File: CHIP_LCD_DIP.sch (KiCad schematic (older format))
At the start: 22 parts, among them CON1 C.H.I.P., CON2 Power, IC1 74LVC138, IC2 DS2431, IC3 AP3032, IC4 74AHC1G08, P1 GPIO, P2 UART, P3 Pwr SW, P5 LCD

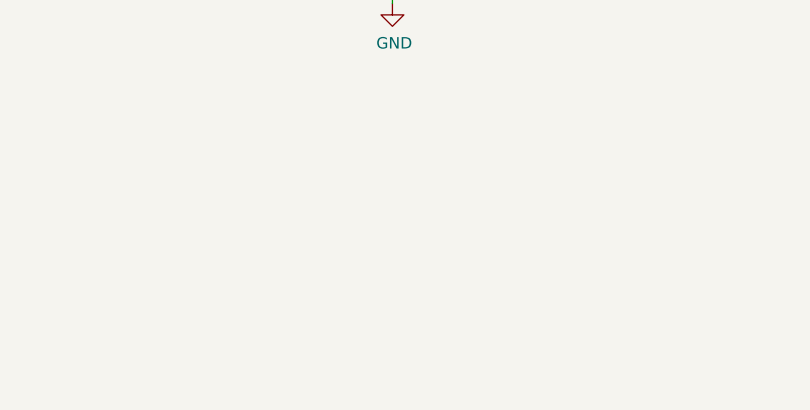
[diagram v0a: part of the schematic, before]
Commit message: Added connector to go to optional capacitive touch board.
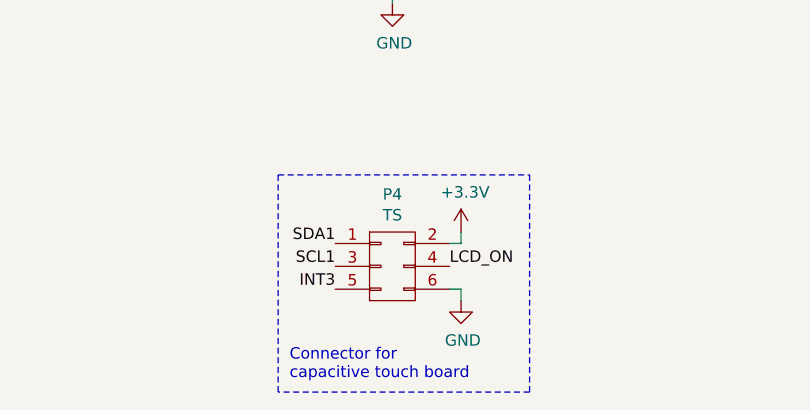
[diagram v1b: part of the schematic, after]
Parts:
- added P4: TS, connectors:02x03_Header_0.05, symbol CONN_02X03
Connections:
- net +3V3: now also P4.2 (P2)
- net GND: now also P4.6 (P6)
- net INT3: now also P4.5 (P5)
- net LCD_ON: now also P4.4 (P4)
- net SCL1: now also P4.3 (P3)
- net SDA1: now also P4.1 (P1)
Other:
- note added: "Connector for\ncapacitive touch board"
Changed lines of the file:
@@
 Sheet 1 1
 Title "C.H.I.P. LCD Adapter & SPI Expander"
-Date "2016-09-01"
-Rev "2"
+Date "2016-09-02"
+Rev "3"
 Comp "Cody Nybo"
 Comment1 ""
@@
 Y2
 $Comp
-L +3.3V #PWR11
+L +3.3V #PWR01
 U 1 1 570D8EAB
 P 3500 5000
-F 0 "#PWR11" H 3500 4850 50  0001 C CNN
+F 0 "#PWR01" H 3500 4850 50  0001 C CNN
 F 1 "+3.3V" H 3518 5174 50  0000 C CNN
 F 2 "" H 3500 5000 60  0000 C CNN
@@
 $EndComp
 $Comp
-L +5V #PWR10
+L +5V #PWR02
 U 1 1 570D8ED5
 P 3250 5000
-F 0 "#PWR10" H 3250 4850 50  0001 C CNN
+F 0 "#PWR02" H 3250 4850 50  0001 C CNN
 F 1 "+5V" H 3268 5174 50  0000 C CNN
 F 2 "" H 3250 5000 60  0000 C CNN
@@
 $EndComp
 $Comp
-L +3.3V #PWR1
+L +3.3V #PWR03
 U 1 1 570D8F46
 P 5200 950
-F 0 "#PWR1" H 5200 800 50  0001 C CNN
+F 0 "#PWR03" H 5200 800 50  0001 C CNN
 F 1 "+3.3V" H 5218 1124 50  0000 C CNN
 F 2 "" H 5200 950 60  0000 C CNN
@@
 $EndComp
 $Comp
-L GND #PWR15
+L GND #PWR04
 U 1 1 570D9535
 P 2250 6000
-F 0 "#PWR15" H 2250 5750 50  0001 C CNN
+F 0 "#PWR04" H 2250 5750 50  0001 C CNN
 F 1 "GND" H 2258 5826 50  0000 C CNN
 F 2 "" H 2250 6000 60  0000 C CNN
@@
 $EndComp
 $Comp
-L GND #PWR6
+L GND #PWR05
 U 1 1 570D971F
 P 5200 2450
-F 0 "#PWR6" H 5200 2200 50  0001 C CNN
+F 0 "#PWR05" H 5200 2200 50  0001 C CNN
 F 1 "GND" H 5208 2276 50  0000 C CNN
 F 2 "" H 5200 2450 60  0000 C CNN
@@
 $EndComp
 $Comp
-L GND #PWR13
+L GND #PWR06
 U 1 1 570E7088
 P 5000 5400
-F 0 "#PWR13" H 5000 5150 50  0001 C CNN
+F 0 "#PWR06" H 5000 5150 50  0001 C CNN
 F 1 "GND" H 5008 5226 50  0000 C CNN
 F 2 "" H 5000 5400 60  0000 C CNN
@@
 $EndComp
 $Comp
-L GND #PWR14
+L GND #PWR07
 U 1 1 570EB8AA
 P 4000 5500
-F 0 "#PWR14" H 4000 5250 50  0001 C CNN
+F 0 "#PWR07" H 4000 5250 50  0001 C CNN
 F 1 "GND" H 4008 5326 50  0000 C CNN
 F 2 "" H 4000 5500 60  0000 C CNN
@@
 Mute
 $Comp
-L +1V8 #PWR12
+L +1V8 #PWR08
 U 1 1 570F8C40
 P 3750 5000
-F 0 "#PWR12" H 3750 4850 50  0001 C CNN
+F 0 "#PWR08" H 3750 4850 50  0001 C CNN
 F 1 "+1V8" H 3768 5174 50  0000 C CNN
 F 2 "" H 3750 5000 60  0000 C CNN
@@
 $EndComp
 $Comp
-L +3.3V #PWR2
+L +3.3V #PWR09
 U 1 1 570F99ED
 P 9050 1500
-F 0 "#PWR2" H 9050 1350 50  0001 C CNN
+F 0 "#PWR09" H 9050 1350 50  0001 C CNN
 F 1 "+3.3V" H 9068 1674 50  0000 C CNN
 F 2 "" H 9050 1500 60  0000 C CNN
@@
 $EndComp
 $Comp
-L GND #PWR9
+L GND #PWR010
 U 1 1 570FA672
 P 8450 4800
-F 0 "#PWR9" H 8450 4550 50  0001 C CNN
+F 0 "#PWR010" H 8450 4550 50  0001 C CNN
 F 1 "GND" H 8458 4626 50  0000 C CNN
 F 2 "" H 8450 4800 60  0000 C CNN
@@
 NoConn ~ 9800 4650
 $Comp
-L GND #PWR4
+L GND #PWR011
 U 1 1 5711414E
 P 9050 1950
-F 0 "#PWR4" H 9050 1700 50  0001 C CNN
+F 0 "#PWR011" H 9050 1700 50  0001 C CNN
 F 1 "GND" H 9058 1776 50  0000 C CNN
 F 2 "" H 9050 1950 60  0000 C CNN
@@
 	1150 1850 1600 1850
 $Comp
-L GND #PWR5
+L GND #PWR012
 U 1 1 5770C9CC
 P 1200 2000
-F 0 "#PWR5" H 1200 1750 50  0001 C CNN
+F 0 "#PWR012" H 1200 1750 50  0001 C CNN
 F 1 "GND" H 1208 1826 50  0000 C CNN
 F 2 "" H 1200 2000 60  0000 C CNN
@@
 Connection ~ 1200 1850
 $Comp
-L +3.3V #PWR3
+L +3.3V #PWR013
 U 1 1 5770D995
 P 1200 1550
-F 0 "#PWR3" H 1200 1400 50  0001 C CNN
+F 0 "#PWR013" H 1200 1400 50  0001 C CNN
 F 1 "+3.3V" H 1218 1724 50  0000 C CNN
 F 2 "" H 1200 1550 60  0000 C CNN
@@
 Connection ~ 8100 4750
 $Comp
-L +3.3V #PWR8
+L +3.3V #PWR014
 U 1 1 57721227
 P 7300 4200
-F 0 "#PWR8" H 7300 4050 50  0001 C CNN
+F 0 "#PWR014" H 7300 4050 50  0001 C CNN
 F 1 "+3.3V" H 7318 4374 50  0000 C CNN
 F 2 "" H 7300 4200 60  0000 C CNN
@@
 XIO3
 $Comp
-L +5V #PWR7
+L +5V #PWR015
 U 1 1 57C03EA0
 P 8100 3600
-F 0 "#PWR7" H 8100 3450 50  0001 C CNN
+F 0 "#PWR015" H 8100 3450 50  0001 C CNN
 F 1 "+5V" H 8118 3774 50  0000 C CNN
 F 2 "" H 8100 3600 60  0000 C CNN
@@
 	1    0    0    -1
 $EndComp
+$Comp
+L CONN_02X03 P4
+U 1 1 57CA09BF
+P 2250 7150
+F 0 "P4" H 2250 7465 50  0000 C CNN
+F 1 "TS" H 2250 7374 50  0000 C CNN
+F 2 "connectors:02x03_Header_0.05" H 2250 7381 60  0001 C CNN
+F 3 "" H 2250 5950 60  0000 C CNN
+	1    2250 7150
+	1    0    0    -1
+$EndComp
+$Comp
+L +3.3V #PWR016
+U 1 1 57CA1873
+P 2550 7000
+F 0 "#PWR016" H 2550 6850 50  0001 C CNN
+F 1 "+3.3V" H 2568 7174 50  0000 C CNN
+F 2 "" H 2550 7000 60  0000 C CNN
+F 3 "" H 2550 7000 60  0000 C CNN
+	1    2550 7000
+	1    0    0    -1
+$EndComp
+$Comp
+L GND #PWR017
+U 1 1 57CA18C0
+P 2550 7300
+F 0 "#PWR017" H 2550 7050 50  0001 C CNN
+F 1 "GND" H 2558 7126 50  0000 C CNN
+F 2 "" H 2550 7300 60  0000 C CNN
+F 3 "" H 2550 7300 60  0000 C CNN
+	1    2550 7300
+	1    0    0    -1
+$EndComp
+Wire Wire Line
+	2500 7250 2550 7250
+Wire Wire Line
+	2550 7250 2550 7300
+Wire Wire Line
+	2500 7050 2550 7050
+Wire Wire Line
+	2550 7050 2550 7000
+Text Label 2000 7050 2    50   ~ 0
+SDA1
+Text Label 2000 7150 2    50   ~ 0
+SCL1
+Text Label 2000 7250 2    50   ~ 0
+INT3
+Text Label 2500 7150 0    50   ~ 0
+LCD_ON
+Wire Notes Line
+	1750 6750 2850 6750
+Wire Notes Line
+	2850 6750 2850 7700
+Wire Notes Line
+	2850 7700 1750 7700
+Wire Notes Line
+	1750 7700 1750 6750
+Text Notes 1800 7650 0    50   ~ 0
+Connector for\ncapacitive touch board
 $EndSCHEMATC

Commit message: Updated files. Added source code. Added pdf copies of design files.
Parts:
- C4: footprint capacitor_smd:C_0805 -> capacitor_smd:C_0603; DigiKey 1276-6457-1-ND -> 1276-1119-1-ND; Package 0805 -> 603; Tolerance 10% -> 20%
- L1: value 6.8µH -> 15µH; Current 490mA -> 400mA; DigiKey 445-174144-1-ND -> 445-6598-1-ND
- P5: DigiKey 609-1195-1-ND -> A100226CT-ND; Manufacturer Amphenol FCI -> TE Connectivity
- R1: value 5.6Ω -> 5.1Ω; DigiKey 311-5.6GRCT-ND -> 311-5.1GRCT-ND
- renumbered CON1 to P1, CON2 to P2, P2 to P4, P1 to P6, P4 to P7
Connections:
- net GND: now also P6.13 (P13); no longer P6.17 (P17)
- net XIO3: now also P6.15 (P15); no longer P6.13 (P13)
- net XIO5: now also P6.17 (P17); no longer P6.15 (P15)
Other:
- note added: "R1:\n5.1Ω for 5" & 7" panel\n15Ω for 4.3" panel"
- note removed: "R1:\n5.6Ω for 5" & 7" panel\n15Ω for 4.3" panel"
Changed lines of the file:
@@
 Sheet 1 1
 Title "C.H.I.P. LCD Adapter & SPI Expander"
-Date "2016-09-02"
-Rev "3"
+Date "2016-10-14"
+Rev "3.1"
 Comp "Cody Nybo"
 Comment1 ""
@@
 $EndDescr
 $Comp
-L CHIP_DIP CON1
+L CHIP_DIP P1
 U 1 1 570CDC11
 P 2350 3500
-F 0 "CON1" H 2350 5937 60  0000 C CNN
+F 0 "P1" H 2350 5937 60  0000 C CNN
 F 1 "C.H.I.P." H 2350 5831 60  0000 C CNN
 F 2 "misc:CHIP_DIP" V 1600 4200 60  0001 C CNN
@@
 P 9200 4600
 F 0 "R1" H 9259 4646 50  0000 L CNN
-F 1 "5.6Ω" H 9259 4554 50  0000 L CNN
+F 1 "5.1Ω" H 9259 4554 50  0000 L CNN
 F 2 "capacitor_smd:C_0603" H 9200 4600 60  0001 C CNN
 F 3 "" H 9200 4600 60  0000 C CNN
-F 4 "311-5.6GRCT-ND" H 9200 4600 60  0001 C CNN "DigiKey"
+F 4 "311-5.1GRCT-ND" H 9200 4600 60  0001 C CNN "DigiKey"
 F 5 "Yageo" H 9200 4600 60  0001 C CNN "Manufacturer"
 F 6 "5%" H 9200 4600 60  0001 C CNN "Tolerance"
@@
 F 1 "LCD" H 10077 3146 50  0000 L CNN
 F 2 "connectors:TE_40_PIN_LCD_Connector" H 10000 3200 60  0001 C CNN
-F 3 "http://portal.fciconnect.com/Comergent//fci/drawing/62684.pdf" H 10000 3200 60  0001 C CNN
-F 4 "609-1195-1-ND" H 10000 3200 60  0001 C CNN "DigiKey"
-F 5 "Amphenol FCI" H 10000 3200 60  0001 C CNN "Manufacturer"
+F 3 "http://www.te.com/commerce/DocumentDelivery/DDEController?Action=srchrtrv&DocNm=1734592&DocType=Customer+Drawing&DocLang=English" H 10000 3200 60  0001 C CNN
+F 4 "A100226CT-ND" H 10000 3200 60  0001 C CNN "DigiKey"
+F 5 "TE Connectivity" H 10000 3200 60  0001 C CNN "Manufacturer"
 F 6 "0.50mm" H 10000 3200 60  0001 C CNN "Pitch"
 F 7 "Bottom" H 10000 3200 60  0001 C CNN "Contacts"
@@
 CS7
 $Comp
-L CONN_01X03 P2
+L CONN_01X03 P4
 U 1 1 570E6A69
 P 5250 5100
-F 0 "P2" H 5328 5138 50  0000 L CNN
+F 0 "P4" H 5328 5138 50  0000 L CNN
 F 1 "UART" H 5328 5046 50  0000 L CNN
 F 2 "Pin_Headers:Pin_Header_Straight_1x03" H 5250 5100 60  0001 C CNN
@@
 	5950 2050 6050 2150
 $Comp
-L CONN_02X17 P1
+L CONN_02X17 P6
 U 1 1 570F253C
 P 5200 3750
-F 0 "P1" H 5200 4766 50  0000 C CNN
+F 0 "P6" H 5200 4766 50  0000 C CNN
 F 1 "GPIO" H 5200 4674 50  0000 C CNN
 F 2 "w_conn_strip:vasch_strip_17x2" H 5200 2650 60  0001 C CNN
@@
 Text Label 5450 3550 0    50   ~ 0
 SCK
+Text Label 4950 3550 2    50   ~ 0
+GND
 Text Label 4950 3750 2    50   ~ 0
-GND
-Text Label 4950 3650 2    50   ~ 0
 XIO5
 Text Label 5450 3750 0    50   ~ 0
@@
 P 8450 3650
 F 0 "L1" H 8450 3865 50  0000 C CNN
-F 1 "6.8µH" H 8450 3774 50  0000 C CNN
+F 1 "15µH" H 8450 3774 50  0000 C CNN
 F 2 "inductor:TDK_VLS-E-CA" H 8350 3650 60  0001 C CNN
-F 3 "https://product.tdk.com/info/en/catalog/datasheets/inductor_automotive_power_vls252008e-ca_en.pdf" H 8450 3750 60  0001 C CNN
-F 4 "445-174144-1-ND" H 8550 3850 50  0001 C CNN "DigiKey"
+F 3 "https://product.tdk.com/info/en/catalog/datasheets/inductor_automotive_power_vls2012e-ca_en.pdf" H 8450 3750 60  0001 C CNN
+F 4 "445-6598-1-ND" H 8550 3850 50  0001 C CNN "DigiKey"
 F 5 "TDK" H 8650 3950 50  0001 C CNN "Manufacturer"
 F 6 "20%" H 8750 4050 50  0001 C CNN "Tolerance"
-F 7 "490mA" H 8850 4150 50  0001 C CNN "Current"
+F 7 "400mA" H 8850 4150 50  0001 C CNN "Current"
 	1    8450 3650
 	1    0    0    -1
@@
 	9800 3450 9650 3450
 Connection ~ 9650 3450
-Text Label 4950 3550 2    50   ~ 0
+Text Label 4950 3650 2    50   ~ 0
 XIO3
 $Comp
@@
 $EndComp
 $Comp
-L BARREL_JACK CON2
+L BARREL_JACK P2
 U 1 1 57C06507
 P 950 5050
-F 0 "CON2" H 931 5397 60  0000 C CNN
+F 0 "P2" H 931 5397 60  0000 C CNN
 F 1 "Power" H 931 5291 60  0000 C CNN
 F 2 "Connect:BARREL_JACK" H 950 5050 60  0001 C CNN
@@
 F 0 "C4" H 9142 1746 50  0000 L CNN
 F 1 "10µF" H 9142 1654 50  0000 L CNN
-F 2 "capacitor_smd:C_0805" H 9050 1700 60  0001 C CNN
+F 2 "capacitor_smd:C_0603" H 9050 1700 60  0001 C CNN
 F 3 "" H 9050 1700 60  0000 C CNN
-F 4 "1276-6457-1-ND" H 9050 1700 60  0001 C CNN "DigiKey"
+F 4 "1276-1119-1-ND" H 9050 1700 60  0001 C CNN "DigiKey"
 F 5 "Samsung" H 9050 1700 60  0001 C CNN "Manufacturer"
 F 6 "6.3V" H 9050 1700 60  0001 C CNN "Voltage"
-F 7 "10%" H 9050 1700 60  0001 C CNN "Tolerance"
+F 7 "20%" H 9050 1700 60  0001 C CNN "Tolerance"
 F 8 "X5R" H 9050 1700 60  0001 C CNN "Temp Co"
-F 9 "0805" H 9050 1700 60  0001 C CNN "Package"
+F 9 "603" H 9050 1700 60  0001 C CNN "Package"
 	1    9050 1700
 	-1   0    0    -1
@@
 Connection ~ 7750 4750
 Text Notes 8700 5050 0    50   ~ 0
-R1:\n5.6Ω for 5" & 7" panel\n15Ω for 4.3" panel
+R1:\n5.1Ω for 5" & 7" panel\n15Ω for 4.3" panel
 Text Notes 700  5300 0    60   ~ 0
 5V In
@@
 $EndComp
 $Comp
-L CONN_02X03 P4
+L CONN_02X03 P7
 U 1 1 57CA09BF
 P 2250 7150
-F 0 "P4" H 2250 7465 50  0000 C CNN
+F 0 "P7" H 2250 7465 50  0000 C CNN
 F 1 "TS" H 2250 7374 50  0000 C CNN
 F 2 "connectors:02x03_Header_0.05" H 2250 7381 60  0001 C CNN
